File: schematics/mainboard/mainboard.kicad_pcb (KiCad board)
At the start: 4 copper layers, 96 x 185 mm, 40 parts, among them J1 SD_Card_Receptacle, J2 Conn_02x20_Odd_Even_MountingP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, J3 USB_C_Receptacle_USB2.0_16P, P1 1-1473005-4, U1 TLV75801PDBV, U2 TLV75801PDBV, U3 MAX3421EETJ_T, U5 BQ24040DSQR, U6 TPS63002, U7 TLV75801PDBV

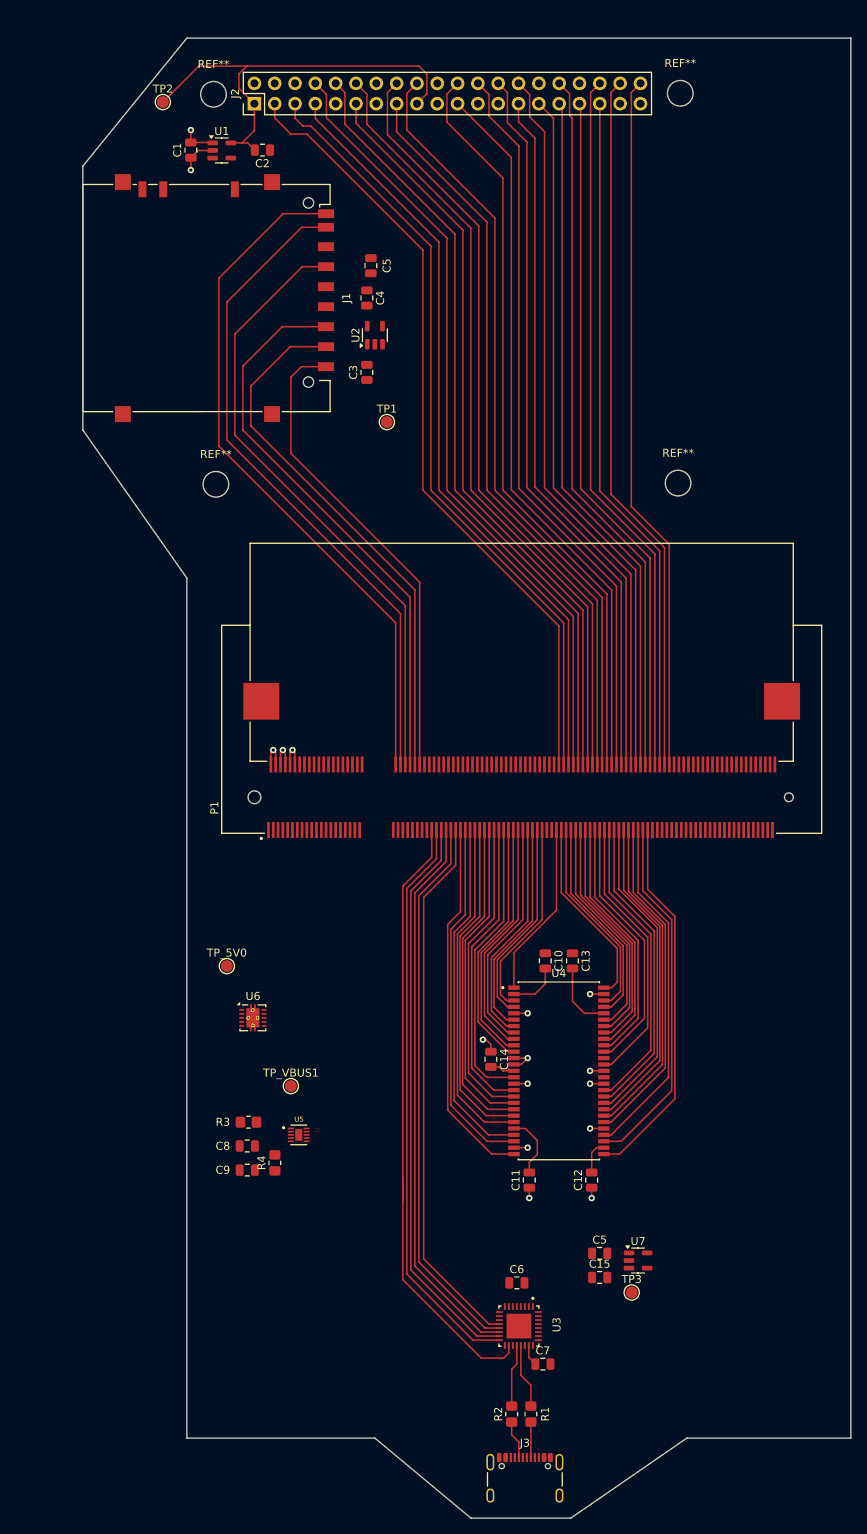
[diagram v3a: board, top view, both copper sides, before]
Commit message: More mainboard schematics work.
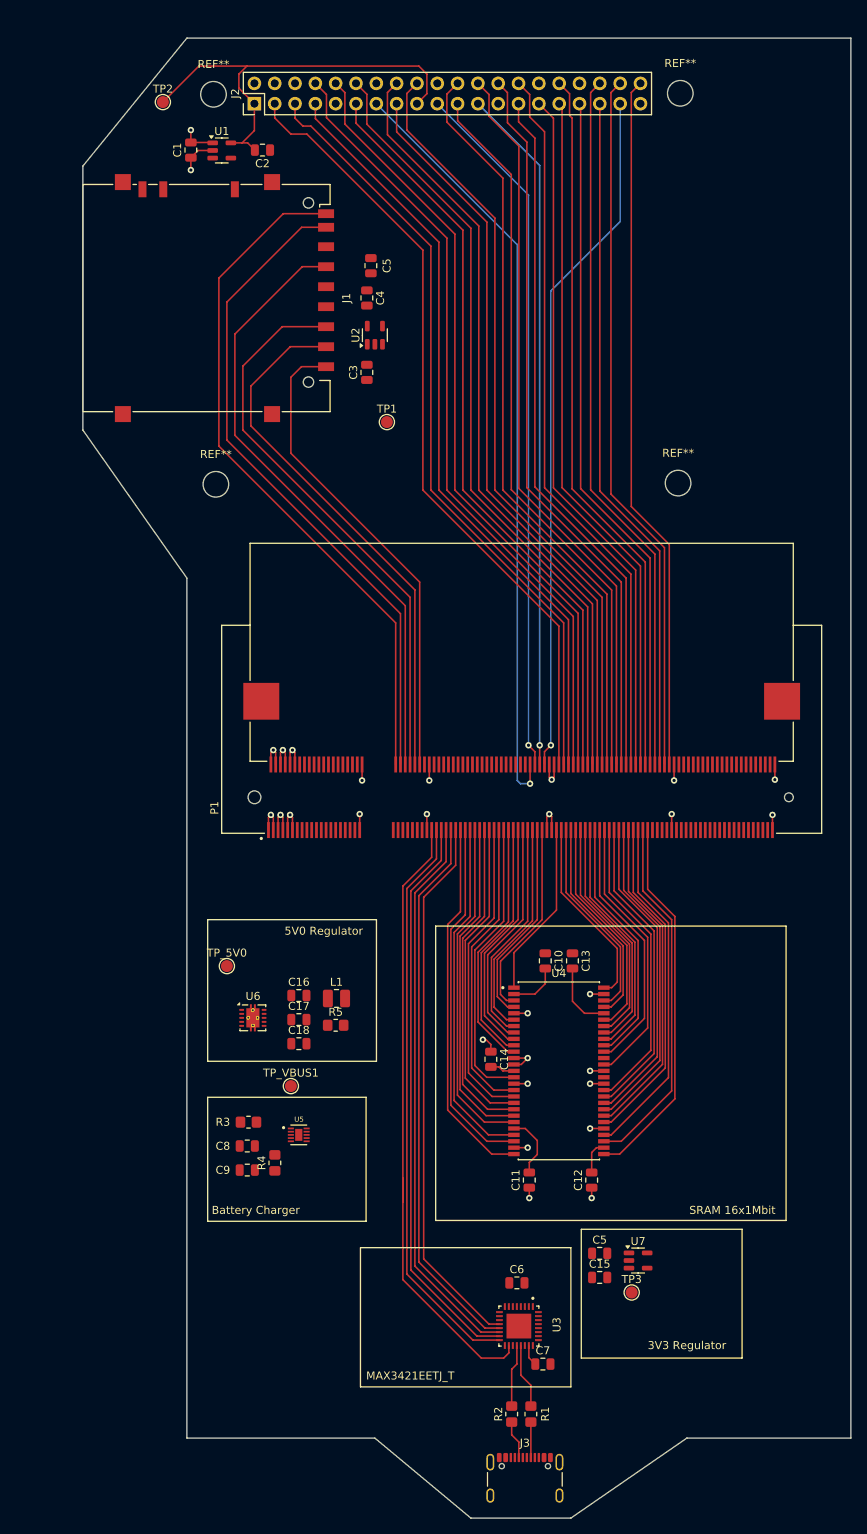
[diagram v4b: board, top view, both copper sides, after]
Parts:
- added C16: 1u, Capacitor_SMD:C_0805_2012Metric, F.Cu at (129.0, 219.7)
- added C17: 10u, Capacitor_SMD:C_0805_2012Metric, F.Cu at (129.0, 222.7)
- added C18: 0.1u, Capacitor_SMD:C_0805_2012Metric, F.Cu at (129.0, 225.7)
- added L1: L, Inductor_SMD:L_1008_2520Metric, F.Cu at (133.7, 220.1)
- added R5: 100, Resistor_SMD:R_0805_2012Metric_Pad1.20x1.40mm_HandSolder, F.Cu at (133.6, 223.4)
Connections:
- P1 pad 100: unconnected-(P1-Pad100) -> LCD_TOUCH_DATA
- P1 pad 102: unconnected-(P1-Pad102) -> LCD_TOUCH_CLK
- P1 pad 104: unconnected-(P1-Pad104) -> LCD_PROG_DATA
- P1 pad 98: unconnected-(P1-Pad98) -> LCD_TOUCH_INTERRUPT
- U6 pad 2: unconnected-(U6-L2-Pad2) -> Net-(U6-L2)
- U6 pad 4: unconnected-(U6-L1-Pad4) -> Net-(U6-L1)
- U6 pad 6: unconnected-(U6-EN-Pad6) -> Net-(U6-EN)
- U6 pad 7: unconnected-(U6-PS/SYNC-Pad7) -> Net-(U6-EN)
- U6 pad 8: unconnected-(U6-VINA-Pad8) -> Net-(U6-EN)
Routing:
- net LCD_TOUCH_INTERRUPT: track 0.00 -> 96.1 mm, vias 0 -> 1
- net LCD_TOUCH_DATA: track 0.00 -> 87.7 mm, vias 0 -> 1
- net LCD_PROG_DATA: track 0.00 -> 86.5 mm, vias 0 -> 1
- net LCD_TOUCH_CLK: track 0.00 -> 85.8 mm, vias 0 -> 1
- net GND: track 25.9 -> 62.2 mm, vias 12 -> 25
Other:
- board text added: "3V3 Regulator"
- board text added: "5V0 Regulator"
- board text added: "Battery Charger"
- board text added: "MAX3421EETJ_T"
- board text added: "SRAM 16x1Mbit"

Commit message: Proper placement of screen on PCB.
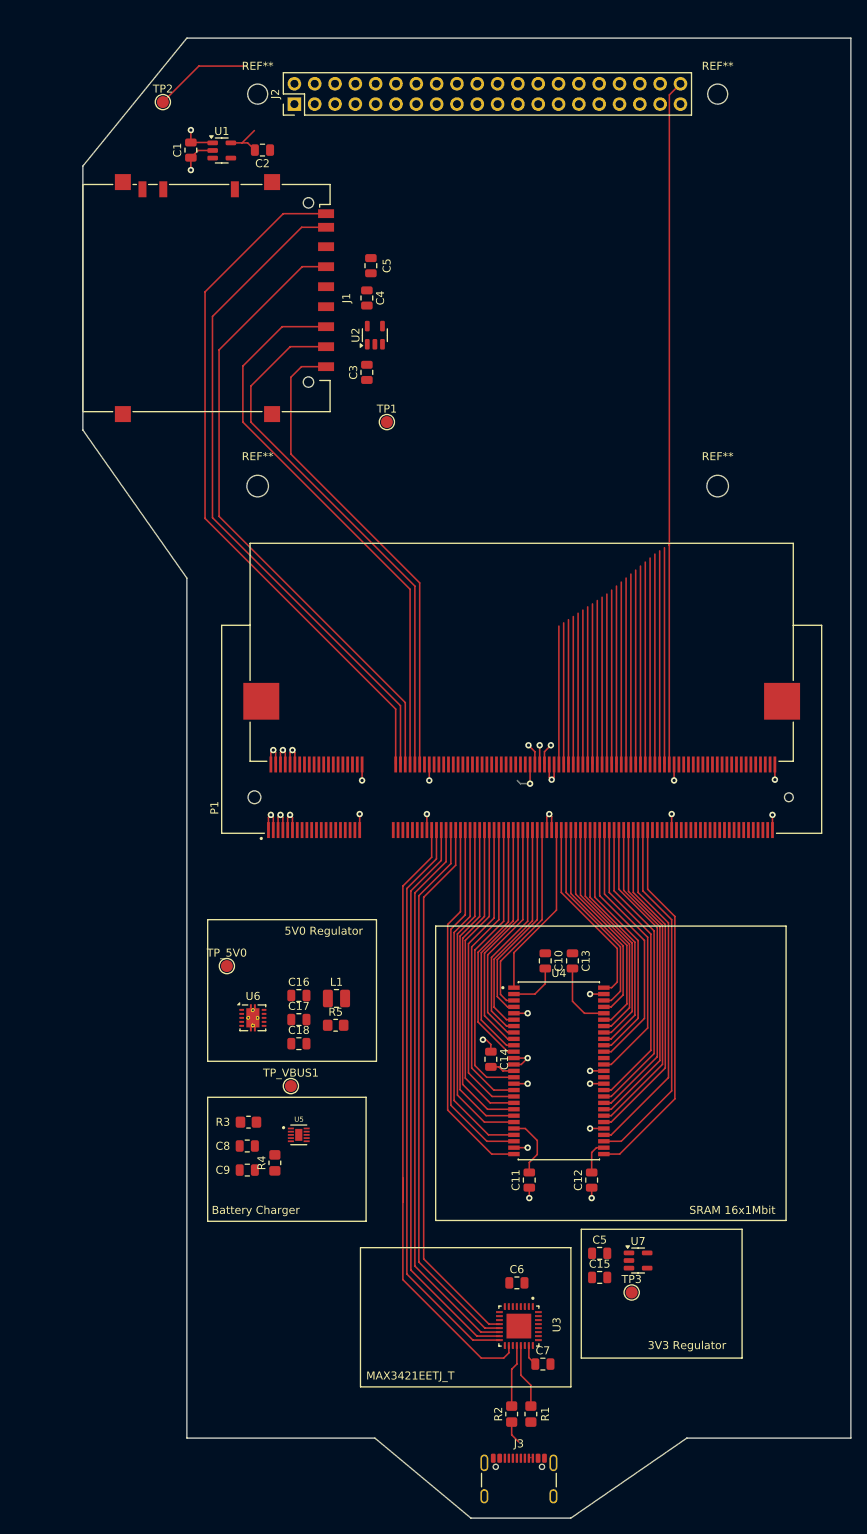
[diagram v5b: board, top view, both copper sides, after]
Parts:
- removed the REF** at (118.6, 155.8)
- removed the REF** at (176.4, 155.6)
- removed the REF** at (176.7, 106.9)
- removed the REF** at (118.3, 107.0)
- added REF**: MountingHole_2.7mm, MountingHole:MountingHole_2.7mm, F.Cu at (123.8, 156.0)
- added REF**: MountingHole_2.5mm, MountingHole:MountingHole_2.5mm, F.Cu at (123.8, 107.0)
- added REF**: MountingHole_2.7mm, MountingHole:MountingHole_2.7mm, F.Cu at (181.3, 156.0)
- added REF**: MountingHole_2.5mm, MountingHole:MountingHole_2.5mm, F.Cu at (181.3, 107.0)
- moved J2 5.00 mm to (128.4, 108.2)
- moved J3 0.75 mm to (156.5, 281.2)
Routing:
- net LCD_TOUCH_INTERRUPT: track 96.1 -> 4.17 mm
- net LCD_TOUCH_DATA: track 87.7 -> 2.73 mm
- net LCD_PROG_DATA: track 86.5 -> 2.73 mm
- net LCD_TOUCH_CLK: track 85.8 -> 2.40 mm
- net LCD_VSYNC: track 98.5 -> 17.3 mm
- net LCD_G2: track 98.5 -> 18.5 mm
- net LCD_HSYNC: track 97.1 -> 17.7 mm
- net LCD_G3: track 97.7 -> 18.9 mm
- net LCD_B0: track 95.7 -> 18.1 mm
- net LCD_CS: track 97.1 -> 19.7 mm
- net LCD_R3: track 96.2 -> 20.1 mm
- net LCD_G5: track 94.3 -> 19.3 mm
- net LCD_R4: track 95.8 -> 20.9 mm
- net LCD_R5: track 94.0 -> 21.3 mm
- net LCD_R2: track 93.0 -> 20.5 mm
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
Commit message: Trace length tuned for LCD and SRAM. Also reduced size of board a bit.
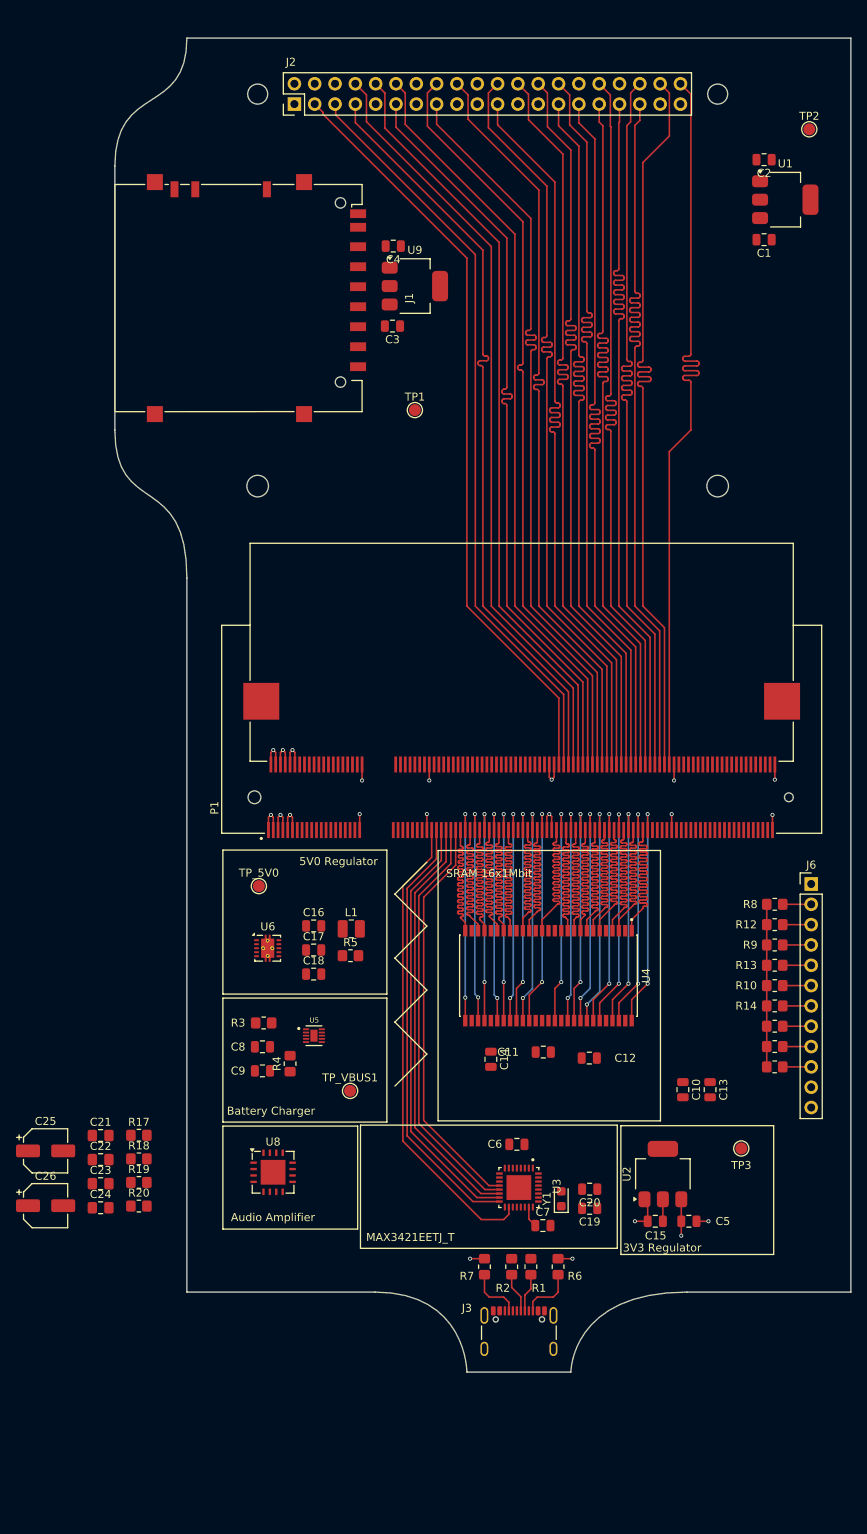
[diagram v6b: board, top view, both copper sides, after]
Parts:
- removed the C5 at (138.0, 128.4)
- removed U7: TLV75801PDBV, Package_TO_SOT_SMD:SOT-23-5
- added C19: C, Capacitor_SMD:C_0805_2012Metric, F.Cu at (165.3, 246.3)
- added C20: C, Capacitor_SMD:C_0805_2012Metric, F.Cu at (165.3, 243.9)
- added C21: 10nF, Capacitor_SMD:C_0805_2012Metric_Pad1.18x1.45mm_HandSolder, F.Cu at (104.2, 237.2)
- added C22: 10nF, Capacitor_SMD:C_0805_2012Metric_Pad1.18x1.45mm_HandSolder, F.Cu at (104.2, 240.2)
- added C23: 10nF, Capacitor_SMD:C_0805_2012Metric_Pad1.18x1.45mm_HandSolder, F.Cu at (104.2, 243.2)
- added C24: 10nF, Capacitor_SMD:C_0805_2012Metric_Pad1.18x1.45mm_HandSolder, F.Cu at (104.2, 246.2)
- added C25: 100uF, Capacitor_SMD:CP_Elec_5x5.3, F.Cu at (97.3, 239.1)
- added C26: 100uF, Capacitor_SMD:CP_Elec_5x5.3, F.Cu at (97.3, 245.9)
- added J6: Conn_01x12, Connector_PinHeader_2.54mm:PinHeader_1x12_P2.54mm_Vertical, F.Cu at (193.0, 205.7)
- added R10: 10k, Resistor_SMD:R_0805_2012Metric_Pad1.20x1.40mm_HandSolder, F.Cu at (188.5, 218.4)
- added R11: 10k, Resistor_SMD:R_0805_2012Metric_Pad1.20x1.40mm_HandSolder, F.Cu at (188.5, 223.5)
- added R12: 10k, Resistor_SMD:R_0805_2012Metric_Pad1.20x1.40mm_HandSolder, F.Cu at (188.5, 210.8)
- added R13: 10k, Resistor_SMD:R_0805_2012Metric_Pad1.20x1.40mm_HandSolder, F.Cu at (188.5, 215.9)
- added R14: 10k, Resistor_SMD:R_0805_2012Metric_Pad1.20x1.40mm_HandSolder, F.Cu at (188.5, 221.0)
- added R15: 10k, Resistor_SMD:R_0805_2012Metric_Pad1.20x1.40mm_HandSolder, F.Cu at (188.5, 226.1)
- added R16: 10k, Resistor_SMD:R_0805_2012Metric_Pad1.20x1.40mm_HandSolder, F.Cu at (188.5, 228.6)
- added R17: 4k7, Resistor_SMD:R_0805_2012Metric_Pad1.20x1.40mm_HandSolder, F.Cu at (109.0, 237.2)
- added R18: 4k7, Resistor_SMD:R_0805_2012Metric_Pad1.20x1.40mm_HandSolder, F.Cu at (109.0, 240.1)
- added R19: 4k7, Resistor_SMD:R_0805_2012Metric_Pad1.20x1.40mm_HandSolder, F.Cu at (109.0, 243.1)
- added R20: 4k7, Resistor_SMD:R_0805_2012Metric_Pad1.20x1.40mm_HandSolder, F.Cu at (109.0, 246.0)
- added R6: 5.1k, Resistor_SMD:R_0805_2012Metric_Pad1.20x1.40mm_HandSolder, F.Cu at (161.4, 253.6)
- added R7: 5.1k, Resistor_SMD:R_0805_2012Metric_Pad1.20x1.40mm_HandSolder, F.Cu at (152.2, 253.6)
- added R8: 10k, Resistor_SMD:R_0805_2012Metric_Pad1.20x1.40mm_HandSolder, F.Cu at (188.5, 208.3)
- added R9: 10k, Resistor_SMD:R_0805_2012Metric_Pad1.20x1.40mm_HandSolder, F.Cu at (188.5, 213.4)
- added U8: MAX9715xTE+, Package_DFN_QFN:TQFN-16-1EP_5x5mm_P0.8mm_EP3.1x3.1mm, F.Cu at (125.8, 241.8)
- added U9: AMS1117-3.3, Package_TO_SOT_SMD:SOT-223-3_TabPin2, F.Cu at (143.5, 131.0)
- added Y1: Crystal, Crystal:Crystal_SMD_2012-2Pin_2.0x1.2mm_HandSoldering, F.Cu at (161.8, 245.1)
- U1, U2: value TLV75801PDBV -> AMS1117-3.3; footprint Package_TO_SOT_SMD:SOT-23-5 -> Package_TO_SOT_SMD:SOT-223-3_TabPin2
- moved U2 110.9 mm to (174.5, 242.0)
- moved TP2 80.9 mm to (192.8, 111.4)
- moved C1 72.5 mm to (187.2, 125.2), turned to 180 degrees
- moved U1 70.7 mm to (189.8, 120.2)
- moved C2 62.7 mm to (187.2, 115.2)
- moved C13 23.6 mm to (180.4, 231.4)
- moved C10 23.6 mm to (177.0, 231.4)
- moved TP3 22.6 mm to (184.3, 238.8), turned to 180 degrees
- moved J3 18.4 mm to (156.5, 262.8)
- moved R1 18.4 mm to (158.0, 253.6)
- moved R2 18.4 mm to (155.6, 253.6)
- moved C6 17.3 mm to (156.2, 238.3)
- moved C7 17.3 mm to (159.5, 248.4)
- moved U3 17.3 mm to (156.5, 243.7)
- moved C11 16.1 mm to (159.6, 226.8), turned to 0 degrees
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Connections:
- C17 pad 2: BAT+ -> SYS_LOAD
- J3 pad A5: unconnected-(J3-CC1-PadA5) -> Net-(J3-CC1)
- J3 pad B5: unconnected-(J3-CC2-PadB5) -> Net-(J3-CC2)
- P1 pad 101: SRAM_D14 -> SRAM_A19
- P1 pad 103: SRAM_D13 -> SRAM_A10
- P1 pad 109: SRAM_D12 -> ~{SRAM_WE}
- P1 pad 111: SRAM_D11 -> ~{SRAM_OE}
- P1 pad 113: SRAM_D10 -> SRAM_A0
- P1 pad 115: SRAM_D9 -> SRAM_A9
- P1 pad 117: SRAM_D8 -> SRAM_A1
- P1 pad 119: SRAM_A5 -> SRAM_A8
- P1 pad 121: SRAM_A6 -> SRAM_A2
- P1 pad 125: SRAM_A8 -> SRAM_A3
- P1 pad 127: SRAM_A9 -> SRAM_A6
- P1 pad 129: ~{SRAM_OE} -> SRAM_A4
- P1 pad 131: SRAM_A10 -> SRAM_A5
- P1 pad 133: SRAM_A11 -> SRAM_D15
- P1 pad 135: SRAM_A12 -> SRAM_D8
- P1 pad 137: SRAM_A13 -> SRAM_D14
- P1 pad 139: SRAM_A14 -> SRAM_D9
- P1 pad 141: SRAM_D7 -> SRAM_D13
- P1 pad 143: SRAM_D6 -> SRAM_D10
- P1 pad 145: SRAM_D5 -> SRAM_D12
- P1 pad 147: SRAM_D4 -> SRAM_D11
- P1 pad 71: SRAM_D2 -> SRAM_D4
- P1 pad 73: SRAM_D1 -> SRAM_D2
- P1 pad 75: SRAM_D0 -> SRAM_D5
- P1 pad 77: SRAM_A15 -> SRAM_D1
- P1 pad 79: SRAM_A16 -> SRAM_D6
- P1 pad 80: unconnected-(P1-Pad80) -> HIO_BTN_X
- P1 pad 81: SRAM_A17 -> SRAM_D0
- P1 pad 82: unconnected-(P1-Pad82) -> HIO_BTN_D
- P1 pad 83: SRAM_A18 -> SRAM_D7
- P1 pad 84: unconnected-(P1-Pad84) -> HIO_BTN_C
- P1 pad 85: SRAM_A19 -> SRAM_A15
- P1 pad 86: unconnected-(P1-Pad86) -> HIO_BTN_B
- P1 pad 87: ~{SRAM_WE} -> SRAM_A14
- P1 pad 88: unconnected-(P1-Pad88) -> HIO_BTN_A
- P1 pad 89: SRAM_A0 -> SRAM_A16
- P1 pad 90: unconnected-(P1-Pad90) -> HIO_DPAD_E
- P1 pad 91: SRAM_A1 -> SRAM_A13
- P1 pad 92: unconnected-(P1-Pad92) -> HIO_DPAD_W
- P1 pad 93: SRAM_A2 -> SRAM_A17
- P1 pad 94: unconnected-(P1-Pad94) -> HIO_DPAD_S
- P1 pad 95: SRAM_A3 -> SRAM_A12
- P1 pad 96: unconnected-(P1-Pad96) -> HIO_DPAD_N
- P1 pad 97: SRAM_A4 -> SRAM_A18
- P1 pad 99: SRAM_D15 -> SRAM_A11
- R5 pad 2: BAT+ -> SYS_LOAD
- U1 pad 1: 5V0 -> GND
- U1 pad 2: GND -> 3V3_LCD
- U1 pad 3: unconnected-(U1-EN-Pad3) -> 5V0
- U2 pad 1: 5V0 -> GND
- U2 pad 2: GND -> 3V3
- U2 pad 3: unconnected-(U2-EN-Pad3) -> 5V0
- U3 pad 24: unconnected-(U3-XI-Pad24) -> USB_HCI_XI
- U3 pad 25: unconnected-(U3-XO-Pad25) -> USB_HCI_XO
- U6 pad 5: BAT+ -> SYS_LOAD
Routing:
- net SD_DAT1: track 88.1 -> 0.00 mm
- net SD_DAT0: track 84.6 -> 0.00 mm
- net SD_CLK: track 79.1 -> 0.00 mm
- net LCD_VSYNC: track 17.3 -> 95.2 mm
- net LCD_G2: track 18.5 -> 96.4 mm
- net LCD_B0: track 18.1 -> 95.5 mm
- net LCD_HSYNC: track 17.7 -> 94.4 mm
- net LCD_G3: track 18.9 -> 95.6 mm
- net LCD_G5: track 19.3 -> 95.0 mm
- net LCD_CS: track 19.7 -> 95.0 mm
- net LCD_R3: track 20.1 -> 95.0 mm
- net LCD_R4: track 20.9 -> 95.6 mm
- net LCD_R5: track 21.3 -> 95.8 mm
- net LCD_R2: track 20.5 -> 94.9 mm
- net LCD_B4: track 22.3 -> 95.3 mm
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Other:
- board size 96 x 185 mm -> 92 x 166.8 mm
- board text added: "Audio Amplifier"

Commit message: More work on mainboard schematic.
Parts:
- removed C8: 1u, Capacitor_SMD:C_0805_2012Metric
- added C27: 10uF, Capacitor_SMD:CP_Elec_5x5.3, F.Cu at (137.4, 240.2)
- added R21: 4k7, Resistor_SMD:R_0805_2012Metric_Pad1.20x1.40mm_HandSolder, F.Cu at (140.8, 123.8)
- added R22: 4k7, Resistor_SMD:R_0805_2012Metric_Pad1.20x1.40mm_HandSolder, F.Cu at (140.8, 121.6)
- added R23: 4k7, Resistor_SMD:R_0805_2012Metric_Pad1.20x1.40mm_HandSolder, F.Cu at (140.8, 142.6)
- added R24: 4k7, Resistor_SMD:R_0805_2012Metric_Pad1.20x1.40mm_HandSolder, F.Cu at (140.8, 140.4)
- added R25: 4k7, Resistor_SMD:R_0805_2012Metric_Pad1.20x1.40mm_HandSolder, F.Cu at (140.8, 138.2)
- C19, C20: value C -> 27pF
- Y1: value Crystal -> 12MHz; footprint Crystal:Crystal_SMD_2012-2Pin_2.0x1.2mm_HandSoldering -> Crystal:Crystal_SMD_HC49-SD
- moved U8 31.8 mm to (126.7, 209.9)
- moved TP_VBUS1 23.4 mm to (118.2, 247.4)
- moved C14 20.4 mm to (160.8, 208.8)
- moved C10 19.6 mm to (172.8, 212.3)
- moved C9 18.8 mm to (131.8, 246.4)
- moved C11 18.8 mm to (147.6, 212.3), turned to -90 degrees
- moved U5 18.5 mm to (131.8, 243.2), turned to -90 degrees
- moved R3 18.1 mm to (132.8, 239.2), turned to -90 degrees
- moved R5 15.9 mm to (136.3, 230.6)
- moved C16 15.9 mm to (131.7, 226.9)
- moved C18 15.9 mm to (131.7, 232.9)
- moved L1 15.9 mm to (136.4, 227.2)
- moved TP_5V0 15.9 mm to (124.8, 221.9)
- moved C17 15.9 mm to (131.7, 229.9)
- moved U6 15.9 mm to (126.0, 229.7)
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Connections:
- U8 pad 14: unconnected-(U8-VDD-Pad14) -> 5V0
- U8 pad 4: Net-(U8-PVDD-Pad4) -> 5V0
- U8 pad 9: Net-(U8-PVDD-Pad4) -> 5V0
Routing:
- net 3V3: track 25.7 -> 155.4 mm
- net 3V3_LCD: track 0.00 -> 94.7 mm
- net SD_CMD: track 0.00 -> 94.5 mm
- net SD_DAT2: track 0.00 -> 94.3 mm
- net SD_DAT1: track 0.00 -> 94.2 mm
- net SD_DAT3: track 0.00 -> 94.2 mm
- net SD_DAT0: track 0.00 -> 92.7 mm
- net SD_CLK: track 0.00 -> 90.1 mm
- net LCD_TOUCH_INTERRUPT: track 0.00 -> 88.9 mm, vias 0 -> 2
- net LCD_PROG_DATA: track 0.00 -> 88.1 mm, vias 0 -> 1
- net LCD_TOUCH_DATA: track 0.00 -> 86.1 mm, vias 0 -> 2
- net LCD_TOUCH_CLK: track 0.00 -> 84.2 mm, vias 0 -> 1
- net HIO_BTN_X: track 3.56 -> 78.9 mm, vias 0 -> 1
- net HIO_BTN_D: track 3.56 -> 76.9 mm, vias 0 -> 1
- net GND: track 45.9 -> 117.7 mm, vias 17 -> 40
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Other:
- board text added: "3V3"
- board text added: "5V"
- board text added: "AUDIO"
- board text added: "BATTERY MANAGEMENT"
- board text added: "USB"
- board text removed: "3V3 Regulator"
- board text removed: "5V0 Regulator"
- board text removed: "Audio Amplifier"
- board text removed: "Battery Charger"
- board text removed: "MAX3421EETJ_T"
